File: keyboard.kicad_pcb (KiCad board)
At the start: 2 copper layers, 203.4 x 107.7 mm, 50 parts, among them J1 TRRS, SW00 Key, SW01 Key, SW02 Key, SW03 Key, SW10 Key, SW11 Key, SW12 Key, SW13 Key, SW14 Key, SW15 Key, SW16 Key, SW17 Key, SW18 Key, SW20 Key, SW21 Key, SW22 Key, SW23 Key, SW24 Key, SW25 Key, SW26 Key, SW27 Key, SW28 Key, SW30 Key, SW31 Key, SW32 Key, SW33 Key, SW34 Key, SW35 Key, SW36 Key, SW37 Key, SW38 Key, SW40 Key, SW41 Key, SW42 Key, SW43 Key, SW44 Key, SW45 Key, SW46 Key, SW47 Key, SW48 Key, U1 ProMicro

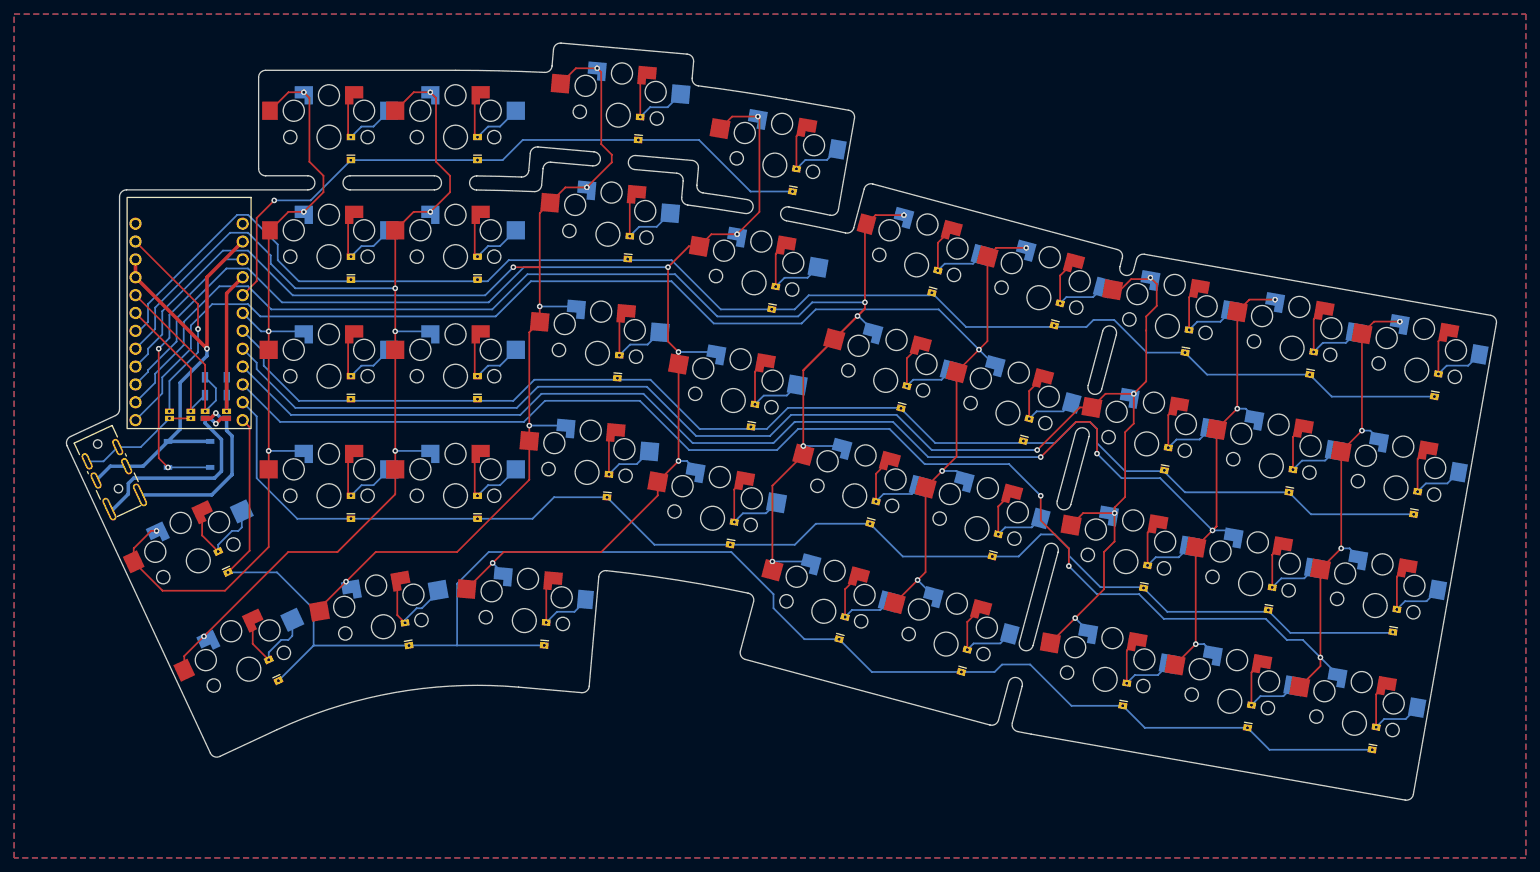
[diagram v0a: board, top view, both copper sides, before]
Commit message: do not have vias on pads
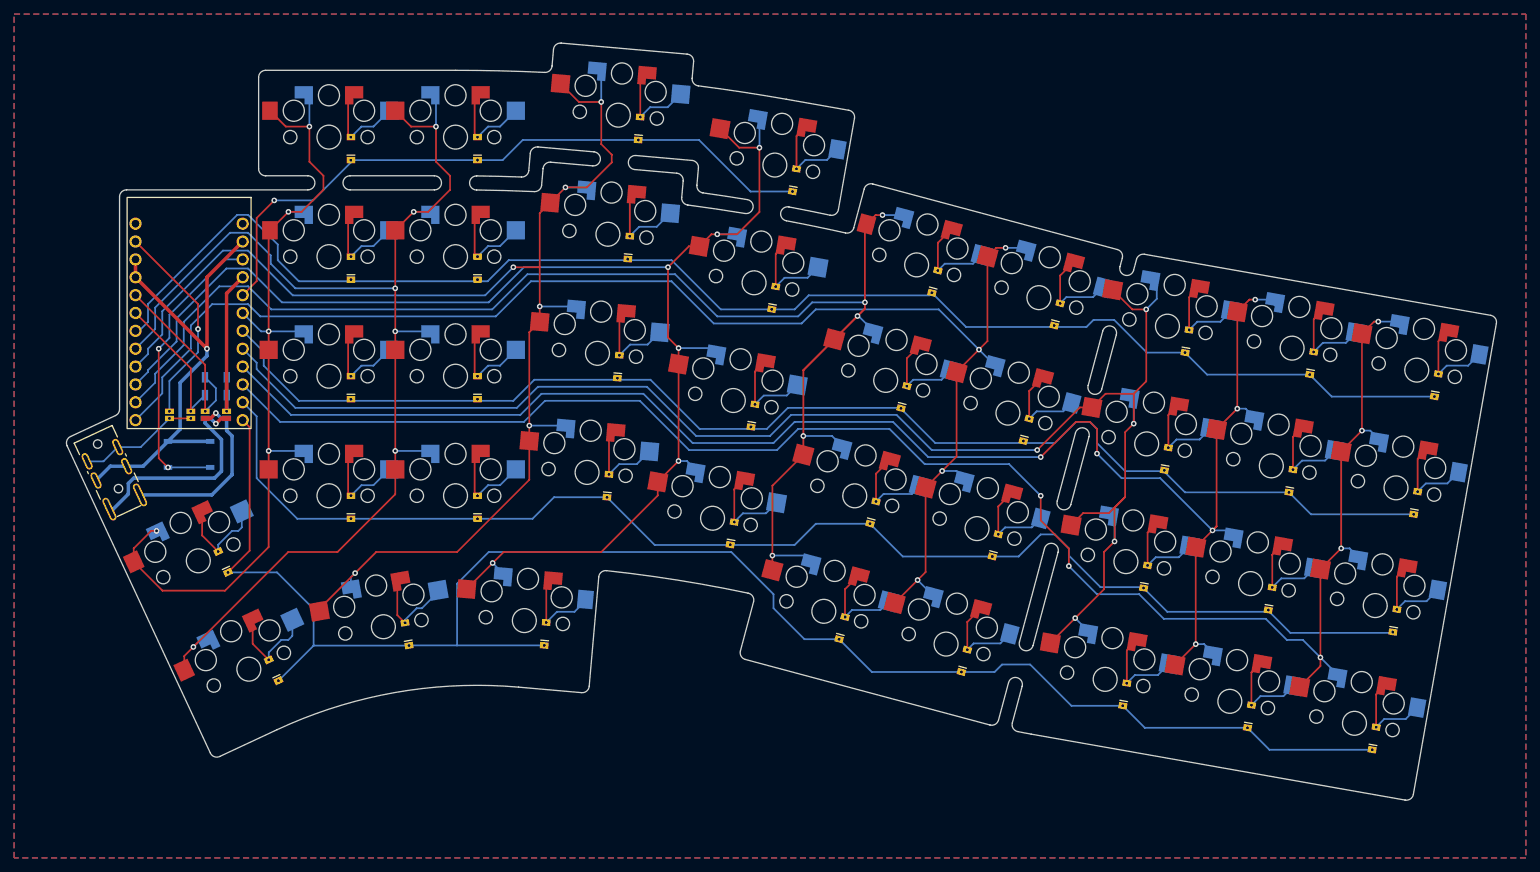
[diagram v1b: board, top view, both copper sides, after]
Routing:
- net col6: track 222.2 -> 229.9 mm
- net col2: track 192.4 -> 197.3 mm
- net col1: track 170.7 -> 175.3 mm
- net col0: track 120.7 -> 123.3 mm
- net col3: track 208.8 -> 210.9 mm
- net col4: track 207.1 -> 208.0 mm

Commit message: make reset button double sided and remove silk screen
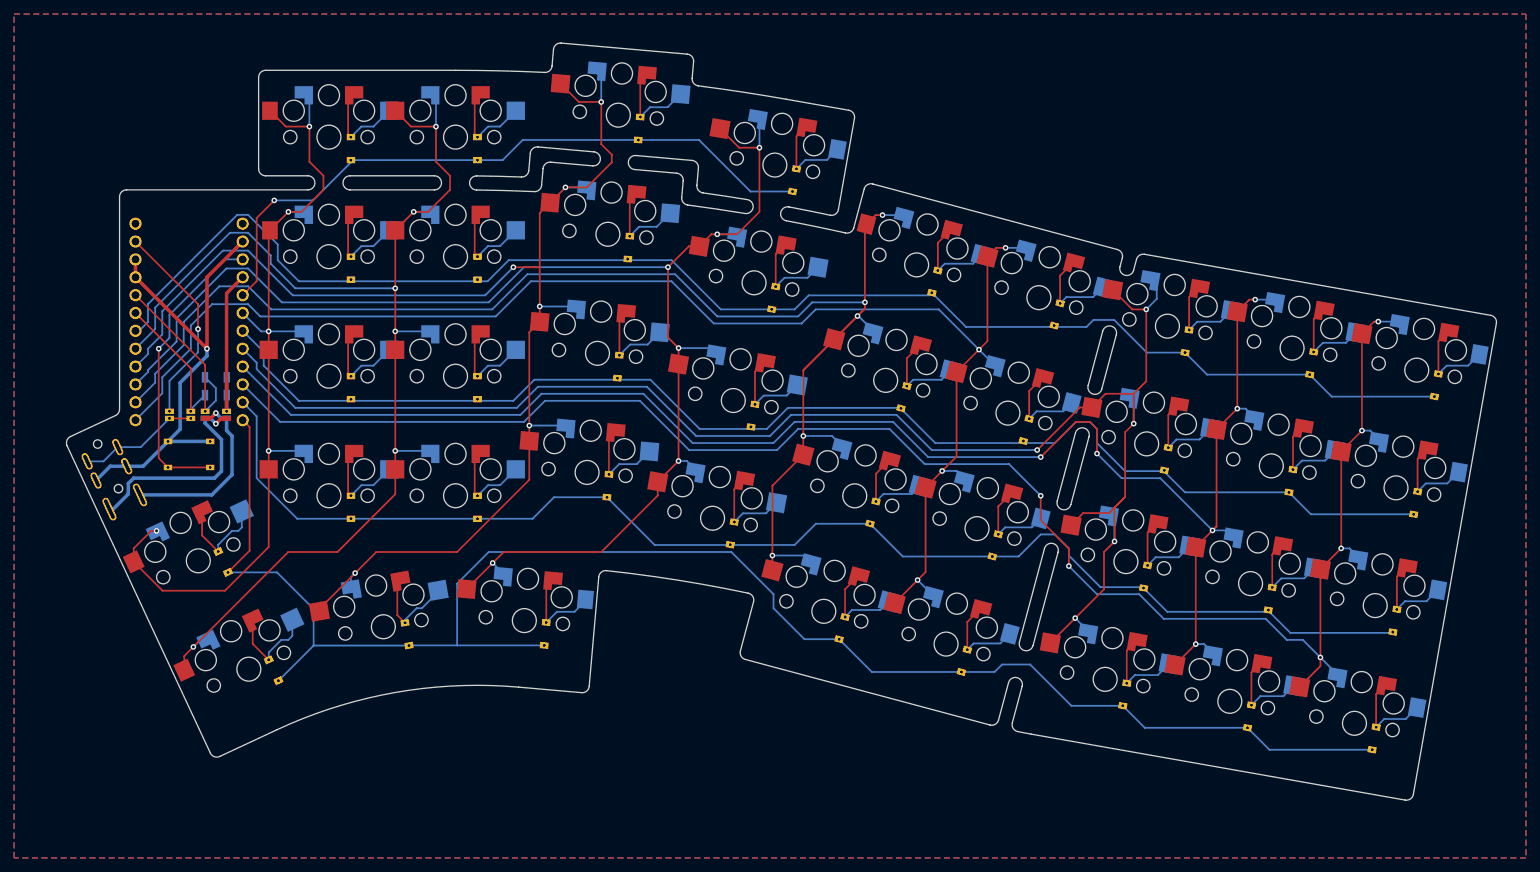
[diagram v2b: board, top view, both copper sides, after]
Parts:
- JP1, JP2: value Jumper -> JumperSplit
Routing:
- net RESET: vias 2 -> 1
